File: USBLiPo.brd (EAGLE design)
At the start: 33 x 15.2 mm, 11 parts, among them IC1 LTC4054, J1 Battery, J2 USB, Q1 2N7002

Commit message: fixed charge current program
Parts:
- LED1: value Red -> Green
- LED2: value Green -> Red
- R3: value 1.3k -> 5.6k
- moved LED1 2.06 mm to (15.2, 2.94)
- moved LED2 2.06 mm to (13.2, 2.94)
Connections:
- net N$1: now also LED2.C; no longer LED1.C
- net N$6: now also LED1.C; no longer LED2.C
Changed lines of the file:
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@@
 <setting verticaltext="up"/>
 </settings>
-<grid distance="12.5" unitdist="mil" unit="mil" style="lines" multiple="1" display="yes" altdistance="3.125" altunitdist="mil" altunit="mil"/>
+<grid distance="12.5" unitdist="mil" unit="mil" style="lines" multiple="1" display="yes" altdistance="1" altunitdist="mil" altunit="mil"/>
 <layers>
 <layer number="1" name="Top" color="4" fill="1" visible="yes" active="yes"/>
@@
 </element>
 <element name="J1" library="freetronics-master-v1" package="S2B-PH" value="Battery" x="29.21" y="7.62" smashed="yes" rot="R270"/>
-<element name="J2" library="freetronics-luke" package="USB-MINIB-FT" value="USB" x="5.08" y="7.62" smashed="yes">
-<attribute name="VALUE" x="5.08" y="1.2382" size="0.8128" layer="27" ratio="15"/>
-</element>
 <element name="F1" library="freetronics-luke" package="1812" value="500mA PTC" x="13.97" y="10.541" smashed="yes">
 <attribute name="VALUE" x="10.668" y="12.573" size="0.8128" layer="27" ratio="15"/>
 </element>
-<element name="R3" library="freetronics" package="0603" value="1.3k" x="19.05" y="5.334" smashed="yes" rot="R270">
+<element name="R3" library="freetronics" package="0603" value="5.6k" x="19.05" y="5.334" smashed="yes" rot="R270">
 <attribute name="VALUE" x="18.288" y="2.794" size="0.8128" layer="27" font="vector" ratio="15" rot="R90"/>
 </element>
-<element name="LED2" library="freetronics-master-v1" package="LED-0603" value="Green" x="15.24" y="2.9369" smashed="yes" rot="R270">
+<element name="LED1" library="freetronics-master-v1" package="LED-0603" value="Green" x="15.24" y="2.9369" smashed="yes" rot="R270">
 <attribute name="NAME" x="14.6812" y="1.4922" size="0.8128" layer="25" ratio="15" rot="SR90"/>
 </element>
-<element name="LED1" library="freetronics-master-v1" package="LED-0603" value="Red" x="13.1763" y="2.9368" smashed="yes" rot="R270">
+<element name="LED2" library="freetronics-master-v1" package="LED-0603" value="Red" x="13.1763" y="2.9368" smashed="yes" rot="R270">
 <attribute name="NAME" x="12.5381" y="1.4923" size="0.8128" layer="25" ratio="15" rot="R90"/>
+</element>
+<element name="J2" library="freetronics-luke" package="USB-MINIB-FT" value="USB" x="5.08" y="7.62" smashed="yes">
+<attribute name="VALUE" x="5.08" y="0.9525" size="0.8128" layer="27" ratio="15"/>
 </element>
 </elements>
@@
 <contactref element="C1" pad="1"/>
 <contactref element="Q1" pad="2"/>
-<contactref element="J2" pad="GND"/>
 <contactref element="R3" pad="2"/>
 <contactref element="J1" pad="1"/>
-<contactref element="J2" pad="SH1"/>
-<contactref element="J2" pad="SH2"/>
-<contactref element="J2" pad="SH3"/>
-<contactref element="J2" pad="SH4"/>
 <via x="18.923" y="8.89" extent="1-16" drill="0.4"/>
 <via x="20.32" y="8.89" extent="1-16" drill="0.4"/>
@@
 <via x="8.255" y="2.8575" extent="1-16" drill="0.6"/>
 <via x="9.525" y="3.175" extent="1-16" drill="0.6"/>
+<contactref element="J2" pad="GND"/>
+<contactref element="J2" pad="SH3"/>
+<contactref element="J2" pad="SH4"/>
+<contactref element="J2" pad="SH1"/>
+<contactref element="J2" pad="SH2"/>
 </signal>
 <signal name="N$1">
 <contactref element="Q1" pad="3"/>
-<contactref element="LED1" pad="C"/>
+<contactref element="LED2" pad="C"/>
 <wire x1="18.499" y1="2.329" x2="21.59" y2="2.329" width="0.6096" layer="1"/>
 <wire x1="11.641" y1="2.329" x2="18.499" y2="2.329" width="0.4572" layer="16"/>
@@
 <signal name="N$8">
 <contactref element="R1" pad="2"/>
+<contactref element="LED1" pad="A"/>
 <contactref element="LED2" pad="A"/>
-<contactref element="LED1" pad="A"/>
 <wire x1="13.1763" y1="3.6988" x2="15.0018" y2="3.6988" width="0.6096" layer="1"/>
 <wire x1="15.0018" y1="3.6988" x2="15.24" y2="3.6989" width="0.4064" layer="1"/>
@@
 </signal>
 <signal name="N$113">
-<contactref element="J2" pad="VBUS"/>
 <contactref element="F1" pad="1"/>
 <wire x1="12.02" y1="10.541" x2="11.969" y2="10.49" width="0.4572" layer="1"/>
@@
 <wire x1="9.271" y1="10.287" x2="11.893" y2="10.287" width="0.6096" layer="1"/>
 <wire x1="11.893" y1="10.287" x2="12.02" y2="10.541" width="0.4572" layer="1"/>
-<wire x1="8.85" y1="9.22" x2="8.85" y2="9.866" width="0.5588" layer="1"/>
+<contactref element="J2" pad="VBUS"/>
+<wire x1="8.85" y1="9.22" x2="8.8392" y2="9.22" width="0.254" layer="1"/>
+<wire x1="8.8392" y1="9.22" x2="8.8392" y2="9.2202" width="0.254" layer="1"/>
+<wire x1="8.8392" y1="9.2202" x2="8.8138" y2="9.2202" width="0.3048" layer="1"/>
+<wire x1="8.8138" y1="9.2202" x2="8.8138" y2="9.2964" width="0.3048" layer="1"/>
+<wire x1="8.8138" y1="9.2964" x2="8.85" y2="9.2964" width="0.6096" layer="1"/>
+<wire x1="8.85" y1="9.2964" x2="8.85" y2="9.866" width="0.6096" layer="1"/>
 </signal>
 <signal name="N$2">
@@
 <contactref element="Q1" pad="1"/>
 <contactref element="R2" pad="2"/>
-<contactref element="LED2" pad="C"/>
+<contactref element="LED1" pad="C"/>
 <wire x1="17.438" y1="5.5" x2="15.875" y2="5.5" width="0.6096" layer="1"/>
 <wire x1="17.438" y1="2.96" x2="17.438" y2="5.5" width="0.6096" layer="1"/>

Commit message: fixed charge current program
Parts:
- Q1: device freetronics-master-v1:SOT23-3 -> freetronics-luke:SOT23-3
- moved Q1 0.06 mm to (21.6, 3.49)
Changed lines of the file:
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@@
 <attribute name="NAME" x="18.161" y="6.604" size="0.8128" layer="25" ratio="15" rot="R90"/>
-</element>
-<element name="Q1" library="freetronics-master-v1" package="SOT23-3" value="2N7002" x="21.59" y="3.429" smashed="yes" rot="R180">
-<attribute name="VALUE" x="19.558" y="0.8255" size="0.8128" layer="27" ratio="15"/>
 </element>
 <element name="R1" library="freetronics" package="0603" value="1k" x="13.208" y="6.35" smashed="yes" rot="R270">
@@
 <attribute name="VALUE" x="5.08" y="0.9525" size="0.8128" layer="27" ratio="15"/>
 </element>
+<element name="Q1" library="freetronics-luke" package="SOT23-3" value="2N7002" x="21.59" y="3.4925" smashed="yes" rot="R180">
+<attribute name="VALUE" x="19.304" y="0.762" size="0.8128" layer="27" ratio="15"/>
+</element>
 </elements>
 <signals>
@@
 <contactref element="IC1" pad="2"/>
 <contactref element="C1" pad="1"/>
-<contactref element="Q1" pad="2"/>
 <contactref element="R3" pad="2"/>
 <contactref element="J1" pad="1"/>
@@
 <contactref element="J2" pad="SH1"/>
 <contactref element="J2" pad="SH2"/>
+<contactref element="Q1" pad="2"/>
 </signal>
 <signal name="N$1">
-<contactref element="Q1" pad="3"/>
 <contactref element="LED2" pad="C"/>
-<wire x1="18.499" y1="2.329" x2="21.59" y2="2.329" width="0.6096" layer="1"/>
 <wire x1="11.641" y1="2.329" x2="18.499" y2="2.329" width="0.4572" layer="16"/>
 <wire x1="11.049" y1="2.921" x2="11.641" y2="2.329" width="0.4572" layer="16"/>
@@
 <via x="18.499" y="2.329" extent="1-16" drill="0.4"/>
 <via x="11.049" y="2.921" extent="1-16" drill="0.4"/>
+<contactref element="Q1" pad="3"/>
+<wire x1="18.499" y1="2.329" x2="21.59" y2="2.329" width="0.4064" layer="1"/>
+<wire x1="21.59" y1="2.329" x2="21.59" y2="2.3925" width="0.4064" layer="1"/>
 </signal>
 <signal name="N$8">
@@
 <signal name="N$6">
 <contactref element="IC1" pad="1"/>
-<contactref element="Q1" pad="1"/>
 <contactref element="R2" pad="2"/>
 <contactref element="LED1" pad="C"/>
@@
 <wire x1="21.59" y1="6.35" x2="21.59" y2="7.9099" width="0.6096" layer="1"/>
 <wire x1="21.59" y1="7.9099" x2="21.6201" y2="7.94" width="0.4572" layer="1"/>
-<wire x1="22.54" y1="5.4" x2="22.54" y2="4.429" width="0.6096" layer="1"/>
 <wire x1="21.59" y1="6.35" x2="22.54" y2="5.4" width="0.6096" layer="1"/>
 <wire x1="17.438" y1="5.5" x2="20.74" y2="5.5" width="0.4572" layer="16"/>
@@
 <via x="17.438" y="5.5" extent="1-16" drill="0.4"/>
 <via x="21.59" y="6.35" extent="1-16" drill="0.4"/>
+<contactref element="Q1" pad="1"/>
+<wire x1="22.54" y1="5.4" x2="22.54" y2="4.4925" width="0.6096" layer="1"/>
 </signal>
 <signal name="N$3">

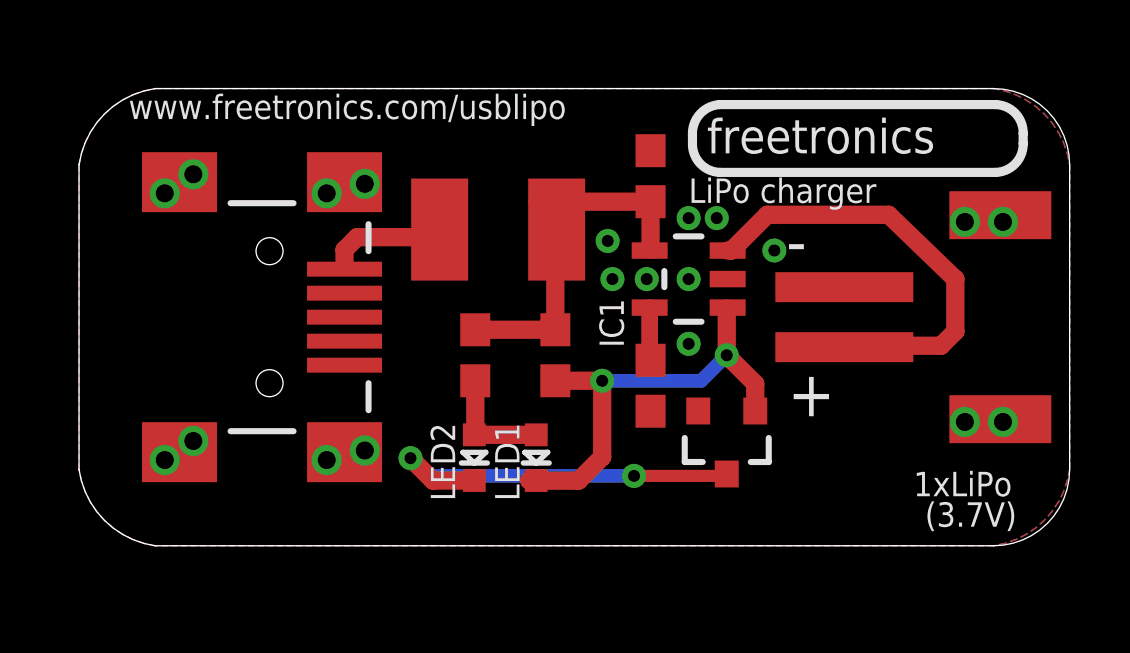
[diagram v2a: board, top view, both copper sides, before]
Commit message: changed JST connector to through-hole right angle
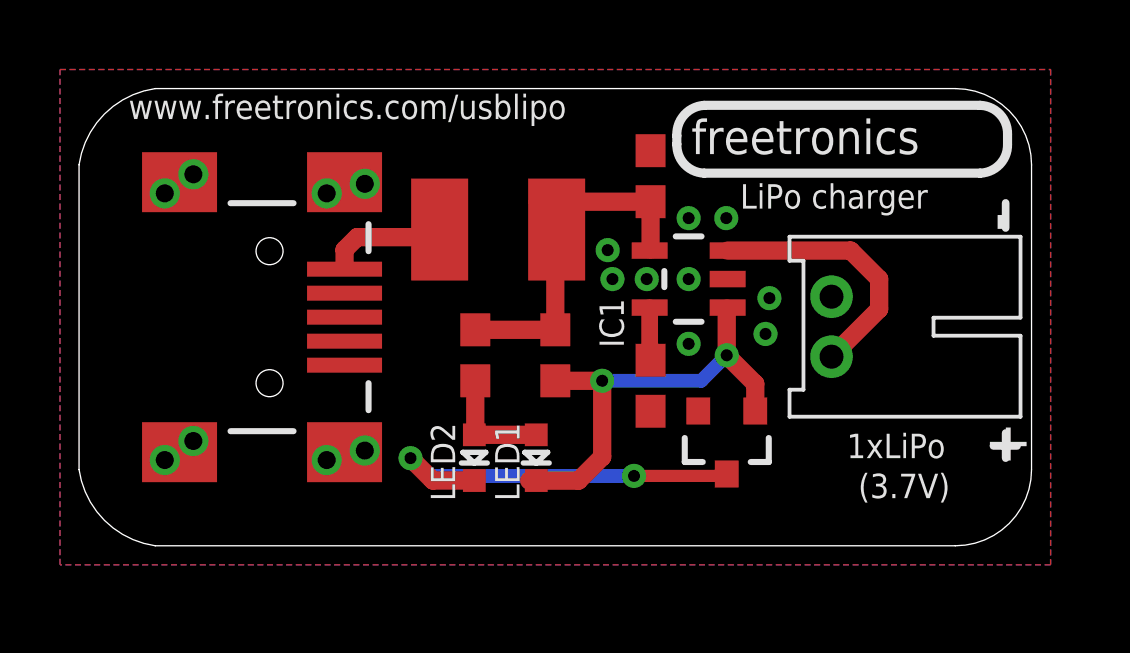
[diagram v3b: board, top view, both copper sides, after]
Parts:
- J1: value Battery -> USB; device freetronics-master-v1:S2B-PH -> freetronics-luke:USB-MINIB-FT
- J2: value USB -> Li cell; device freetronics-luke:USB-MINIB-FT -> adafruit:JST-PH-2-THM-RA
- moved J1 24.1 mm to (5.08, 7.62), turned to 0 degrees
- moved J2 20.0 mm to (25.1, 7.30), turned to 270 degrees
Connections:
- net GND: now also J1.GND, J1.SH1, J1.SH2, J1.SH3, J1.SH4, J2.2; no longer J1.1, J2.GND, J2.SH1, J2.SH2, J2.SH3, J2.SH4
- net N$113: now also J1.VBUS; no longer J2.VBUS
- net N$4: now also J2.1; no longer J1.2
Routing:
- net N$4: track 14.6 -> 8.69 mm
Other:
- board size 33 x 15.2 mm -> 31.8 x 15.2 mm
- board text removed: "+"
- board text removed: "-"

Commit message: foo
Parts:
- removed J2: Li cell, adafruit:JST-PH-2-THM-RA
- added B1: LiPo cell, freetronics-luke:JST-2MM-TH-RA
- added R4, R5: 10k, freetronics:0603
- added S1, S2: SJ, freetronics-luke:SJ
- LED1: value Green -> Charge
- LED2: value Red -> Standby
- R3: value 5.6k -> 3k3
- moved R3 5.94 mm to (24.4, 2.86), turned to 90 degrees
- moved C1 4.07 mm to (23.1, 12.1), turned to 180 degrees
- moved LED1 0.63 mm to (15.9, 2.94)
- moved LED2 0.63 mm to (12.5, 2.94)
- moved F1 0.32 mm to (14.0, 10.2)
- moved R1 0.32 mm to (13.2, 6.03)
- moved R2 0.32 mm to (15.9, 6.03)
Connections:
- new net N$5: R3.1, S1.1
- new net N$7: R4.1, S2.1
- net GND: now also B1.-, R4.2, R5.2; no longer J2.2
- net N$3: now also R5.1, S1.2, S2.2; no longer R3.1
- net N$4: now also B1.+; no longer J2.1
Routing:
- net N$3: track 1.77 -> 22.6 mm, vias 0 -> 2
- net N$7: track 0.00 -> 7.49 mm
- net N$4: track 8.69 -> 15.2 mm, vias 0 -> 2
- net GND: track 0.00 -> 4.60 mm, vias 17 -> 18
- net N$2: track 14.0 -> 17.8 mm
- net N$5: track 0.00 -> 2.28 mm
- net N$1: track 13.3 -> 11.5 mm
- net N$8: track 3.88 -> 5.25 mm
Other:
- board size 31.8 x 15.2 mm -> 31.8 x 15.9 mm
- board text added: "+"
- board text added: "-"
- board text added: "0 0 100 mA"
- board text added: "0 1 200 mA"
- board text added: "0= open"
- board text added: "1 0 303 mA"
- board text added: "1 1 503 mA"
- board text added: "1= short"
- board text added: "Charging"
- board text added: "S1"
- board text added: "S1 S2 Charge Current"
- board text added: "S2"
- board text added: "Standby"

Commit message: foo
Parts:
- R1: value 1k -> 10k
- R2: value 10k -> 1k
- moved R1 2.67 mm to (15.9, 6.03)
- moved R2 2.67 mm to (13.2, 6.03)
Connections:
- net N$6: now also R1.2; no longer R2.2
- net N$8: now also R2.2; no longer R1.2
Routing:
- net N$4: vias 2 -> 3
- net GND: vias 18 -> 19
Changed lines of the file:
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@@
 <setting verticaltext="up"/>
 </settings>
-<grid distance="12.5" unitdist="mil" unit="mil" style="lines" multiple="1" display="yes" altdistance="2.5" altunitdist="mil" altunit="mil"/>
+<grid distance="6.25" unitdist="mil" unit="mil" style="lines" multiple="1" display="yes" altdistance="2.5" altunitdist="mil" altunit="mil"/>
 <layers>
 <layer number="1" name="Top" color="4" fill="1" visible="yes" active="yes"/>
@@
 <elements>
 <element name="IC1" library="freetronics-luke" package="SOT23-5" value="LTC4054" x="20.32" y="8.89" smashed="yes" rot="R90"/>
-<element name="R1" library="freetronics" package="0603" value="1k" x="13.208" y="6.0325" smashed="yes" rot="R270"/>
-<element name="R2" library="freetronics" package="0603" value="10k" x="15.875" y="6.0325" smashed="yes" rot="R270"/>
+<element name="R2" library="freetronics" package="0603" value="1k" x="13.208" y="6.0325" smashed="yes" rot="R270"/>
+<element name="R1" library="freetronics" package="0603" value="10k" x="15.875" y="6.0325" smashed="yes" rot="R270"/>
 <element name="C1" library="freetronics" package="0603" value="1uF" x="23.114" y="12.065" smashed="yes" rot="R180"/>
 <element name="F1" library="freetronics-luke" package="1812" value="500mA PTC" x="13.97" y="10.2235" smashed="yes"/>
@@
 <via x="17.653" y="7.9375" extent="1-16" drill="0.4"/>
 <via x="28.2575" y="8.5725" extent="1-16" drill="0.4"/>
-<via x="29.21" y="8.5725" extent="1-16" drill="0.4"/>
+<via x="29.36875" y="8.5725" extent="1-16" drill="0.4"/>
+<via x="30.48" y="8.5725" extent="1-16" drill="0.4"/>
 </signal>
 <signal name="N$1">
@@
 <wire x1="12.5413" y1="3.6988" x2="15.9543" y2="3.6988" width="0.6096" layer="1"/>
 <wire x1="15.9543" y1="3.6988" x2="15.875" y2="3.6989" width="0.4064" layer="1"/>
-<contactref element="R1" pad="2"/>
+<contactref element="R2" pad="2"/>
 <wire x1="12.5413" y1="3.6988" x2="12.5413" y2="4.5158" width="0.6096" layer="1"/>
 <wire x1="12.5413" y1="4.5158" x2="13.208" y2="5.1825" width="0.6096" layer="1"/>
@@
 </signal>
 <signal name="N$2">
+<contactref element="R2" pad="1"/>
 <contactref element="R1" pad="1"/>
-<contactref element="R2" pad="1"/>
 <contactref element="IC1" pad="4"/>
 <contactref element="C1" pad="2"/>
@@
 <signal name="N$6">
 <contactref element="IC1" pad="1"/>
-<contactref element="R2" pad="2"/>
+<contactref element="R1" pad="2"/>
 <contactref element="LED1" pad="C"/>
 <wire x1="17.438" y1="2.96" x2="17.438" y2="5.1952" width="0.6096" layer="1"/>
@@
 <wire x1="26.67" y1="9.525" x2="26.67" y2="7.3025" width="0.6096" layer="1"/>
 <wire x1="25.9875" y1="6.62" x2="26.67" y2="7.3025" width="0.6096" layer="1"/>
-<wire x1="28.2575" y1="6.6675" x2="29.21" y2="6.6675" width="1.524" layer="16"/>
+<wire x1="28.2575" y1="6.6675" x2="29.36875" y2="6.6675" width="1.524" layer="16"/>
 <via x="28.2575" y="6.6675" extent="1-16" drill="0.4"/>
-<via x="29.21" y="6.6675" extent="1-16" drill="0.4"/>
-<wire x1="29.21" y1="6.6675" x2="30.48" y2="6.6675" width="1.524" layer="16"/>
+<via x="29.36875" y="6.6675" extent="1-16" drill="0.4"/>
+<wire x1="29.36875" y1="6.6675" x2="30.48" y2="6.6675" width="1.524" layer="16"/>
 <wire x1="25.0825" y1="6.62" x2="28.21" y2="6.62" width="0.8128" layer="16"/>
 <wire x1="28.21" y1="6.62" x2="28.2575" y2="6.6675" width="0.6096" layer="16"/>
 <wire x1="25.9875" y1="6.62" x2="25.0825" y2="6.62" width="0.6096" layer="1"/>
+<via x="30.48" y="6.6675" extent="1-16" drill="0.4"/>
 </signal>
 <signal name="N$5">

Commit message: Layout and overlay
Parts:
- removed J1: USB, freetronics-luke:USB-MINIB-FT
- added X1: USBSF-MICROB, freetronics-jon:USB-MICROB
- B1: value LiPo cell -> 2P-JST-PTH; device freetronics-luke:JST-2MM-TH-RA -> freetronics-jon:FREETRONICS-LUKE_JST-2MM-TH-RA
- moved C1 9.18 mm to (14.0, 12.9)
- moved LED2 6.96 mm to (5.59, 2.54), turned to 0 degrees
- moved R1 6.74 mm to (9.14, 6.35)
- moved R2 6.10 mm to (7.11, 6.35)
- moved F1 5.36 mm to (8.64, 10.8)
- moved R3 5.09 mm to (19.4, 3.17)
- moved S1 5.09 mm to (21.6, 2.86)
- moved IC1 5.09 mm to (15.2, 9.21)
- moved R5 5.09 mm to (14.0, 5.65)
- moved Q1 5.09 mm to (16.5, 3.81)
- moved R4 5.09 mm to (16.8, 1.11)
- moved S2 5.09 mm to (24.4, 2.86)
- moved B1 4.76 mm to (24.1, 7.62)
- moved LED1 4.21 mm to (11.7, 2.54), turned to 0 degrees
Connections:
- net GND: now also B1.NEG, X1.FIX1, X1.FIX2, X1.GND, X1.TAB1, X1.TAB2; no longer B1.-, J1.GND, J1.SH1, J1.SH2, J1.SH3, J1.SH4
- net N$113: now also X1.VBUS; no longer J1.VBUS
- net N$4: now also B1.POS; no longer B1.+
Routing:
- net N$4: track 15.2 -> 9.47 mm, vias 3 -> 0
- net N$8: track 5.25 -> 9.39 mm
- net N$2: track 17.8 -> 14.5 mm
- net GND: track 4.60 -> 5.92 mm, vias 19 -> 18
- net N$6: track 15.4 -> 15.9 mm
- net N$1: track 11.5 -> 11.3 mm, vias 2 -> 0
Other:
- board size 31.8 x 15.9 mm -> 26.7 x 15.2 mm
- board text added: "CHARGE"
- board text added: "IN"
- board text added: "OUT"
- board text added: "STANDBY"
- board text removed: "Charging"
- board text removed: "Standby"

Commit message: Overlay and values
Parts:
- R1, R4, R5: value 10k -> 10K
- R2: value 1k -> 1K
- R3: value 3k3 -> 3K3
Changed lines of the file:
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@@
 <elements>
 <element name="IC1" library="freetronics-luke" package="SOT23-5" value="LTC4054" x="15.24" y="9.2075" smashed="yes" rot="R90"/>
-<element name="R2" library="freetronics" package="0603" value="1k" x="7.112" y="6.35" smashed="yes" rot="R270"/>
-<element name="R1" library="freetronics" package="0603" value="10k" x="9.144" y="6.35" smashed="yes" rot="R270"/>
+<element name="R2" library="freetronics" package="0603" value="1K" x="7.112" y="6.35" smashed="yes" rot="R270"/>
+<element name="R1" library="freetronics" package="0603" value="10K" x="9.144" y="6.35" smashed="yes" rot="R270"/>
 <element name="C1" library="freetronics" package="0603" value="1uF" x="13.97" y="12.8905" smashed="yes" rot="R180"/>
 <element name="F1" library="freetronics-luke" package="1812" value="500mA PTC" x="8.636" y="10.795" smashed="yes"/>
-<element name="R5" library="freetronics" package="0603" value="10k" x="13.97" y="5.6515" smashed="yes" rot="R270"/>
+<element name="R5" library="freetronics" package="0603" value="10K" x="13.97" y="5.6515" smashed="yes" rot="R270"/>
 <element name="LED1" library="freetronics-master-v1" package="LED-0603" value="Charge" x="11.684" y="2.54" smashed="yes"/>
 <element name="LED2" library="freetronics-master-v1" package="LED-0603" value="Standby" x="5.588" y="2.54" smashed="yes"/>
 <element name="Q1" library="freetronics-luke" package="SOT23-3" value="2N7002" x="16.51" y="3.81" smashed="yes" rot="R180"/>
-<element name="R3" library="freetronics" package="0603" value="3k3" x="19.3675" y="3.175" smashed="yes" rot="R90"/>
-<element name="R4" library="freetronics" package="0603" value="10k" x="16.8275" y="1.11125" smashed="yes" rot="R180"/>
+<element name="R3" library="freetronics" package="0603" value="3K3" x="19.3675" y="3.175" smashed="yes" rot="R90"/>
+<element name="R4" library="freetronics" package="0603" value="10K" x="16.8275" y="1.11125" smashed="yes" rot="R180"/>
 <element name="S1" library="freetronics-luke" package="SJ" value="SJ" x="21.59" y="2.8575" smashed="yes" rot="R90"/>
 <element name="S2" library="freetronics-luke" package="SJ" value="SJ" x="24.4475" y="2.8575" smashed="yes" rot="R90"/>
